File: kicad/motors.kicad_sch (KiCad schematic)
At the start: 71 parts, among them J12 Conn_01x04_Pin, J3 Conn_01x04_Pin, J4 Conn_01x04_Pin, J5 Conn_01x04_Pin, J6 Conn_01x04_Pin, U3 TMC2209-LA, U4 TMC2209-LA, U5 TMC2209-LA, U6 TMC2100-LA

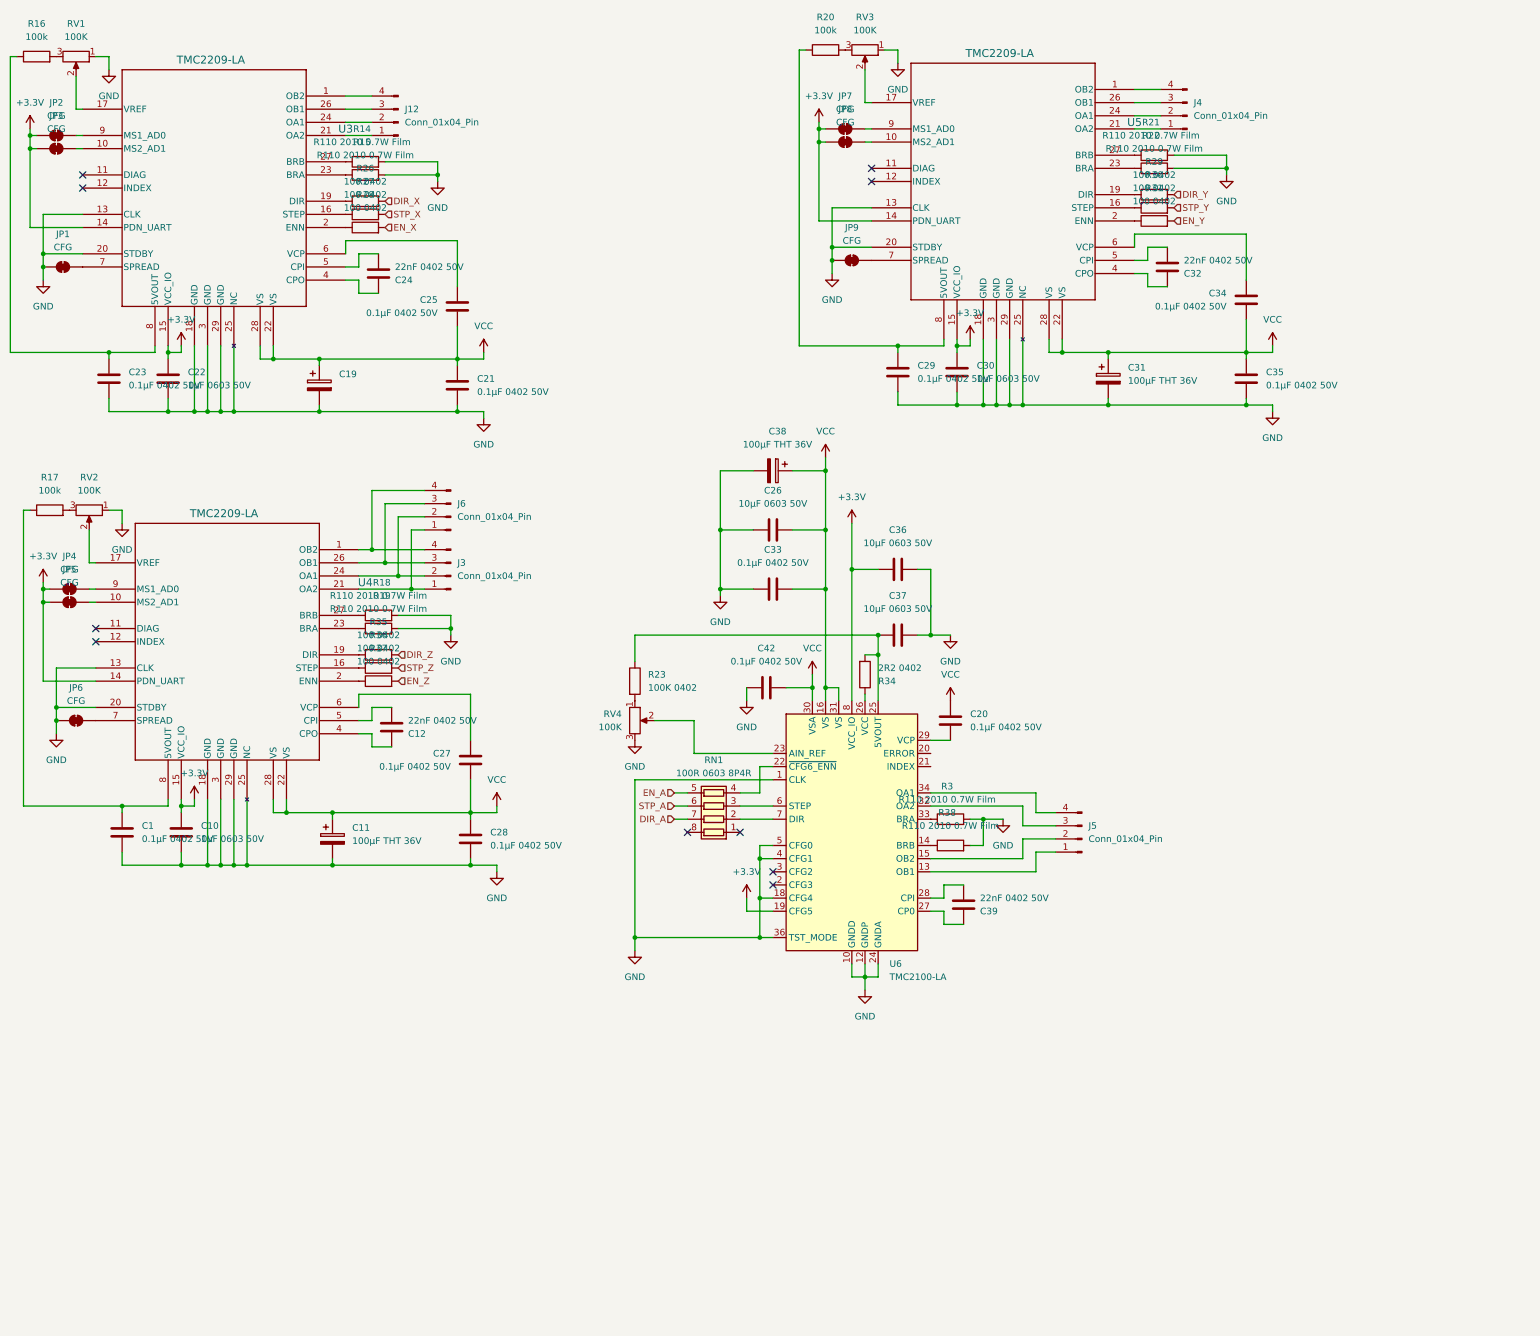
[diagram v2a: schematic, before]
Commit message: DRV8825 schematic
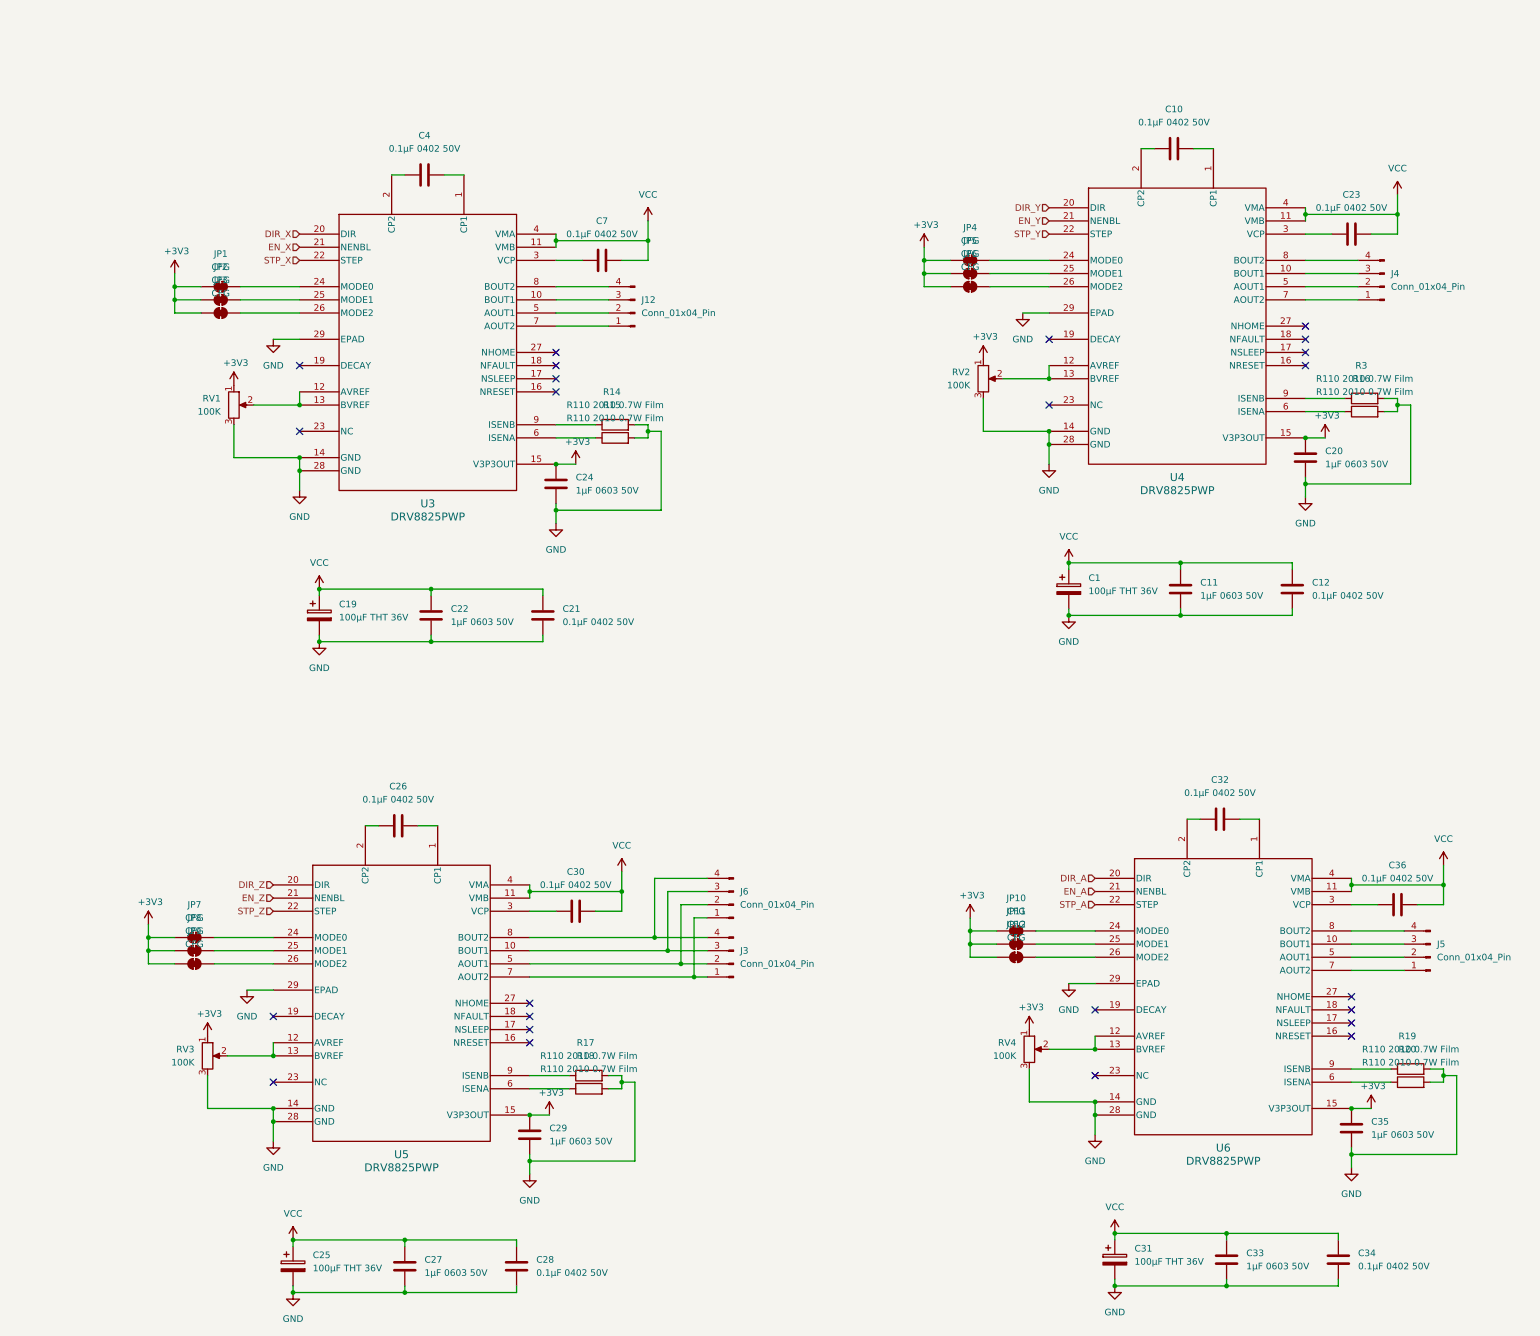
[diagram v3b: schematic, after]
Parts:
- removed C1, C25, C42: 0.1μF 0402 50V, Capacitor_SMD:C_0402_1005Metric, symbol Device:C
- removed C11, C38: 100μF THT 36V, Capacitor_THT:C_Radial_D6.3mm_H11.0mm_P2.50mm, symbol Device:C_Polarized
- removed C37: 10μF 0603 50V, Capacitor_SMD:C_0402_1005Metric, symbol Device:C
- removed C39: 22nF 0402 50V, Capacitor_SMD:C_0402_1005Metric, symbol Device:C
- removed R21, R22, R38: R110 2010 0.7W Film, Resistor_SMD:R_2010_5025Metric, symbol Device:R
- removed R23: 100K 0402, Resistor_SMD:R_0402_1005Metric, symbol Device:R
- removed R26, R27, R28, R29, R30, R31, R35, R36, R37: 100 0402, Resistor_SMD:R_0402_1005Metric, symbol Device:R
- removed R34: 2R2 0402, Resistor_SMD:R_0402_1005Metric, symbol Device:R
- removed RN1: 100R 0603 8P4R, Resistor_SMD:R_Array_Concave_4x0603, symbol Device:R_Pack04
- removed U3, U4, U5: TMC2209-LA, rephat-parts:QFN28_5X5_TRI-M, symbol rephat-symbols:TMC2209-LA
- removed U6: TMC2100-LA, Package_DFN_QFN:QFN-36-1EP_5x6mm_P0.5mm_EP3.6x4.1mm_ThermalVias, symbol Driver_Motor:TMC2100-LA
- added C1, C25: 100μF THT 36V, Capacitor_THT:C_Radial_D6.3mm_H11.0mm_P2.50mm, symbol Device:C_Polarized
- added C11: 1μF 0603 50V, Capacitor_SMD:C_0402_1005Metric, symbol Device:C
- added C4, C7: 0.1μF 0402 50V, Capacitor_SMD:C_0402_1005Metric, symbol Device:C
- added JP10, JP11, JP12: CFG, Jumper:SolderJumper-2_P1.3mm_Bridged_RoundedPad1.0x1.5mm, symbol Jumper:SolderJumper_2_Bridged
- added U3, U4, U5, U6: DRV8825PWP, Package_SO:HTSSOP-28-1EP_4.4x9.7mm_P0.65mm_EP3.4x9.5mm_ThermalVias, symbol rephat-symbols:DRV8825PWP
- C10, C30: value 1μF 0603 50V -> 0.1μF 0402 50V
- C12, C32: value 22nF 0402 50V -> 0.1μF 0402 50V
- C20, C27, C29, C33, C35: value 0.1μF 0402 50V -> 1μF 0603 50V
- C24: value 22nF 0402 50V -> 1μF 0603 50V
- C26, C36: value 10μF 0603 50V -> 0.1μF 0402 50V
- R16, R17, R20: value 100k -> R110 2010 0.7W Film; footprint Resistor_SMD:R_0402_1005Metric -> Resistor_SMD:R_2010_5025Metric
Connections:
- net DIR_A: now also U6.20 (DIR)
- net DIR_X: now also U3.20 (DIR)
- net DIR_Y: now also U4.20 (DIR)
- net DIR_Z: now also U5.20 (DIR)
- net EN_A: now also U6.21 (NENBL)
- net EN_X: now also U3.21 (NENBL)
- net EN_Y: now also U4.21 (NENBL)
- net EN_Z: now also U5.21 (NENBL)
- net GND: now also C12.2, C20.2, C24.2, C27.2, C33.2, C34.2, R16.2, R17.2, R20.2, RV1.3, RV2.3, RV3.3, C1.2, C11.2, C25.2, U3.14 (GND), U3.28 (GND), U3.29 (EPAD), U4.14 (GND), U4.28 (GND), U4.29 (EPAD), U5.14 (GND), U5.28 (GND), U5.29 (EPAD), U6.14 (GND), U6.28 (GND), U6.29 (EPAD); no longer C10.2, C23.2, C26.1, C30.2, C33.1, C36.2, JP1.1 (A), JP6.1 (A), JP9.1 (A), RV1.1, RV2.1, RV3.1
- net STP_A: now also U6.22 (STEP)
- net STP_X: now also U3.22 (STEP)
- net STP_Y: now also U4.22 (STEP)
- net STP_Z: now also U5.22 (STEP)
- net VCC: now also C12.1, C22.1, C23.2, C30.2, C33.1, C36.2, C1.1, C11.1, C25.1, C7.2, U3.11 (VMB), U3.4 (VMA), U4.11 (VMB), U4.4 (VMA), U5.11 (VMB), U5.4 (VMA), U6.11 (VMB), U6.4 (VMA); no longer C20.2, C26.2, C33.2, C35.1
- net at R17.1: now also U5.9 (ISENB)
- net at R3.1: now also U4.9 (ISENB)
- net at J3.1 (Pin_1), J6.1 (Pin_1): now also U5.7 (AOUT2)
- net at J3.2 (Pin_2), J6.2 (Pin_2): now also U5.5 (AOUT1)
- net at J3.3 (Pin_3), J6.3 (Pin_3): now also U5.10 (BOUT1)
- net at J3.4 (Pin_4), J6.4 (Pin_4): now also U5.8 (BOUT2)
- net at JP7.2 (B): now also U5.24 (MODE0)
- net at RV3.2: now also U5.12 (AVREF), U5.13 (BVREF)
- net at RV1.2: now also U3.12 (AVREF), U3.13 (BVREF)
- net at R19.1: now also U6.9 (ISENB)
- net at JP6.2 (B): now also U4.26 (MODE2)
- net at C32.1: now also U6.2 (CP2)
- net at C32.2: now also U6.1 (CP1)
- net at R15.1: now also U3.6 (ISENA)
- net at JP1.2 (B): now also U3.24 (MODE0)
- net at C23.1: now also U4.3 (VCP); no longer R16.1
- net at R20.1: now also U6.6 (ISENA); no longer C29.1
- net +3V3: now reaches C20.1
- net +3V3: now also C24.1, C29.1, C35.1, JP1.1 (A), JP2.1 (A), JP3.1 (A), JP4.1 (A), JP5.1 (A), JP6.1 (A), JP7.1 (A), JP8.1 (A), JP9.1 (A), RV1.1, RV2.1, RV3.1, RV4.1, JP10.1 (A), JP11.1 (A), JP12.1 (A), U3.15 (V3P3OUT), U4.15 (V3P3OUT), U5.15 (V3P3OUT), U6.15 (V3P3OUT)
- net at J12.4 (Pin_4): now also U3.8 (BOUT2)
- net at JP3.2 (B): now also U3.26 (MODE2)
- net at J12.1 (Pin_1): now also U3.7 (AOUT2)
- net at J12.2 (Pin_2): now also U3.5 (AOUT1)
- net at J12.3 (Pin_3): now also U3.10 (BOUT1)
- net at R14.1: now also U3.9 (ISENB)
- net at JP2.2 (B): now also U3.25 (MODE1)
- net at JP5.2 (B): now also U4.25 (MODE1)
- net at RV2.2: now also U4.12 (AVREF), U4.13 (BVREF)
- net at R18.1: now also U5.6 (ISENA)
- net at JP4.2 (B): now also U4.24 (MODE0)
- net at JP8.2 (B): now also U5.25 (MODE1)
- net at J4.1 (Pin_1): now also U4.7 (AOUT2)
- net at J4.2 (Pin_2): now also U4.5 (AOUT1)
- net at J4.3 (Pin_3): now also U4.10 (BOUT1)
- net at J4.4 (Pin_4): now also U4.8 (BOUT2)
- net at RV4.2: now also U6.12 (AVREF), U6.13 (BVREF)
- net at J5.1 (Pin_1): now also U6.7 (AOUT2)
- net at J5.2 (Pin_2): now also U6.5 (AOUT1)
- net at J5.3 (Pin_3): now also U6.10 (BOUT1)
- net at J5.4 (Pin_4): now also U6.8 (BOUT2)
- net at JP9.2 (B): now also U5.26 (MODE2)
- removed net +3.3V: C10.1, C22.1, C30.1, C36.1, JP2.1 (A), JP3.1 (A), JP4.1 (A), JP5.1 (A), JP7.1 (A), JP8.1 (A)
- new net: C36.1, U6.3 (VCP)
- new net: C10.1, U4.2 (CP2)
- new net: C10.2, U4.1 (CP1)
- new net: C30.1, U5.3 (VCP)
- new net: C26.1, U5.2 (CP2)
- new net: C26.2, U5.1 (CP1)
- new net: JP10.2 (B), U6.24 (MODE0)
- new net: R16.1, U4.6 (ISENA)
- new net: JP11.2 (B), U6.25 (MODE1)
- new net: C4.1, U3.2 (CP2)
- new net: C4.2, U3.1 (CP1)
- new net: JP12.2 (B), U6.26 (MODE2)
- new net: C7.1, U3.3 (VCP)
- no-connect marks 10 -> 24
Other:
- moved on the sheet: C19, C21, C22, J12, J3, J4, J5, J6, RV1

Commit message: PCB redo
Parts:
- R14, R15, R16, R17, R18, R19, R20, R3: value R110 2010 0.7W Film -> R100 0603; footprint Resistor_SMD:R_2010_5025Metric -> Resistor_SMD:R_0603_1608Metric
- RV1, RV2, RV3, RV4: value 100K -> 10K
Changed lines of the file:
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@@
 			)
 		)
-		(property "Value" "100K"
+		(property "Value" "10K"
 			(at 62.23 93.9799 0)
 			(effects
@@
 			)
 		)
-		(property "Value" "R110 2010 0.7W Film"
+		(property "Value" "R100 0603"
 			(at 138.43 92.71 90)
 			(effects
@@
 			)
 		)
-		(property "Footprint" "Resistor_SMD:R_2010_5025Metric"
+		(property "Footprint" "Resistor_SMD:R_0603_1608Metric"
 			(at 138.43 98.298 90)
 			(effects
@@
 			)
 		)
-		(property "Value" "100K"
+		(property "Value" "10K"
 			(at 57.15 219.7099 0)
 			(effects
@@
 			)
 		)
-		(property "Value" "R110 2010 0.7W Film"
+		(property "Value" "R100 0603"
 			(at 133.35 218.44 90)
 			(effects
@@
 			)
 		)
-		(property "Footprint" "Resistor_SMD:R_2010_5025Metric"
+		(property "Footprint" "Resistor_SMD:R_0603_1608Metric"
 			(at 133.35 224.028 90)
 			(effects
@@
 			)
 		)
-		(property "Value" "100K"
+		(property "Value" "10K"
 			(at 215.9 218.4399 0)
 			(effects
@@
 			)
 		)
-		(property "Value" "R110 2010 0.7W Film"
+		(property "Value" "R100 0603"
 			(at 133.35 220.98 90)
 			(effects
@@
 			)
 		)
-		(property "Footprint" "Resistor_SMD:R_2010_5025Metric"
+		(property "Footprint" "Resistor_SMD:R_0603_1608Metric"
 			(at 133.35 226.568 90)
 			(effects
@@
 			)
 		)
-		(property "Value" "R110 2010 0.7W Film"
+		(property "Value" "R100 0603"
 			(at 138.43 95.25 90)
 			(effects
@@
 			)
 		)
-		(property "Footprint" "Resistor_SMD:R_2010_5025Metric"
+		(property "Footprint" "Resistor_SMD:R_0603_1608Metric"
 			(at 138.43 100.838 90)
 			(effects
@@
 			)
 		)
-		(property "Value" "R110 2010 0.7W Film"
+		(property "Value" "R100 0603"
 			(at 292.1 219.71 90)
 			(effects
@@
 			)
 		)
-		(property "Footprint" "Resistor_SMD:R_2010_5025Metric"
+		(property "Footprint" "Resistor_SMD:R_0603_1608Metric"
 			(at 292.1 225.298 90)
 			(effects
@@
 			)
 		)
-		(property "Value" "R110 2010 0.7W Film"
+		(property "Value" "R100 0603"
 			(at 283.21 90.17 90)
 			(effects
@@
 			)
 		)
-		(property "Footprint" "Resistor_SMD:R_2010_5025Metric"
+		(property "Footprint" "Resistor_SMD:R_0603_1608Metric"
 			(at 283.21 95.758 90)
 			(effects
@@
 			)
 		)
-		(property "Value" "R110 2010 0.7W Film"
+		(property "Value" "R100 0603"
 			(at 292.1 217.17 90)
 			(effects
@@
 			)
 		)
-		(property "Footprint" "Resistor_SMD:R_2010_5025Metric"
+		(property "Footprint" "Resistor_SMD:R_0603_1608Metric"
 			(at 292.1 222.758 90)
 			(effects
@@
 			)
 		)
-		(property "Value" "R110 2010 0.7W Film"
+		(property "Value" "R100 0603"
 			(at 283.21 87.63 90)
 			(effects
@@
 			)
 		)
-		(property "Footprint" "Resistor_SMD:R_2010_5025Metric"
+		(property "Footprint" "Resistor_SMD:R_0603_1608Metric"
 			(at 283.21 93.218 90)
 			(effects
@@
 			)
 		)
-		(property "Value" "100K"
+		(property "Value" "10K"
 			(at 207.01 88.8999 0)
 			(effects

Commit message: schematic candidate 0
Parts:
- added RN1, RN2, RN3, RN4: 100R 4x0603, Resistor_SMD:R_Array_Concave_4x0603, symbol Device:R_Pack04
- J12, J3, J4, J5, J6: footprint Connector_JST:JST_XH_B4B-XH-A_1x04_P2.50mm_Vertical -> rephat-parts:S4B-XH-SM4-TB
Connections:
- net DIR_A: now also RN4.6 (R3.2); no longer U6.20 (DIR)
- net DIR_X: now also RN2.6 (R3.2); no longer U3.20 (DIR)
- net DIR_Y: now also RN1.6 (R3.2); no longer U4.20 (DIR)
- net DIR_Z: now also RN3.6 (R3.2); no longer U5.20 (DIR)
- net EN_A: now also RN4.7 (R2.2); no longer U6.21 (NENBL)
- net EN_X: now also RN2.7 (R2.2); no longer U3.21 (NENBL)
- net EN_Y: now also RN1.7 (R2.2); no longer U4.21 (NENBL)
- net EN_Z: now also RN3.7 (R2.2); no longer U5.21 (NENBL)
- net STP_A: now also RN4.8 (R1.2); no longer U6.22 (STEP)
- net STP_X: now also RN2.8 (R1.2); no longer U3.22 (STEP)
- net STP_Y: now also RN1.8 (R1.2); no longer U4.22 (STEP)
- net STP_Z: now also RN3.8 (R1.2); no longer U5.22 (STEP)
- new net: RN4.1 (R1.1), U6.22 (STEP)
- new net: RN4.2 (R2.1), U6.21 (NENBL)
- new net: RN4.3 (R3.1), U6.20 (DIR)
- new net: RN3.1 (R1.1), U5.22 (STEP)
- new net: RN3.2 (R2.1), U5.21 (NENBL)
- new net: RN3.3 (R3.1), U5.20 (DIR)
- new net: RN1.1 (R1.1), U4.22 (STEP)
- new net: RN1.2 (R2.1), U4.21 (NENBL)
- new net: RN1.3 (R3.1), U4.20 (DIR)
- new net: RN2.1 (R1.1), U3.22 (STEP)
- new net: RN2.2 (R2.1), U3.21 (NENBL)
- new net: RN2.3 (R3.1), U3.20 (DIR)
- no-connect marks 24 -> 32
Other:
- moved on the sheet: C1, C10, C11, C12, C19, C20, C21, C22, C23, C24, C25, C26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

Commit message: Toshiba TB67S109A stepper driver
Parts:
- removed C35: 1μF 0603 50V, Capacitor_SMD:C_0402_1005Metric, symbol Device:C
- removed C36: 0.1μF 0402 50V, Capacitor_SMD:C_0402_1005Metric, symbol Device:C
- removed R20: R100 0603, Resistor_SMD:R_0603_1608Metric, symbol Device:R
- removed RV4: 10K, Potentiometer_SMD:Potentiometer_Bourns_TC33X_Vertical, symbol Device:R_Potentiometer
- removed U6: DRV8825PWP, Package_SO:HTSSOP-28-1EP_4.4x9.7mm_P0.65mm_EP3.4x9.5mm_ThermalVias, symbol rephat-symbols:DRV8825PWP
- added D6: LED, LED_SMD:LED_0603_1608Metric, symbol Device:LED
- added R11: 20K 0402, Resistor_SMD:R_0402_1005Metric, symbol Device:R
- added R13: 200Ω 0402, Resistor_SMD:R_0402_1005Metric, symbol Device:R
- added RV5: 10K, Potentiometer_SMD:Potentiometer_Bourns_TC33X_Vertical, symbol Device:R_Potentiometer
- added U6: TB67S109AFTG, Package_DFN_QFN:QFN-48-1EP_7x7mm_P0.5mm_EP5.45x5.45mm_ThermalVias, symbol rephat-symbols:TB67S109AFTG
- C32: value 0.1μF 0402 50V -> 100 pF 0402 50V
- R19: value R100 0603 -> 100K 0402; footprint Resistor_SMD:R_0603_1608Metric -> Resistor_SMD:R_0402_1005Metric
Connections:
- net DIR_A: now also RN4.7 (R2.2); no longer RN4.6 (R3.2)
- net EN_A: now also RN4.8 (R1.2); no longer RN4.7 (R2.2)
- net GND: now also C32.2, U6.15 (GND), U6.18 (GND), U6.19 (GND), U6.22 (GND), U6.4 (RESET), U6.40 (GND), U6.5 (GND); no longer R19.2
- net STP_A: now also RN4.6 (R3.2); no longer RN4.8 (R1.2)
- net VCC: now also U6.32 (VM)
- net at RN4.1 (R1.1): now also U6.3 (ENABLE)
- net at RN4.2 (R2.1): now also U6.44 (CW/CCW)
- net at RN4.3 (R3.1): now also U6.2 (CLK)
- net at JP10.2 (B): now also U6.39 (DMODE0)
- net +5V: now reaches R19.1
- net +5V: now also D6.2 (A), R11.1, U6.34 (VCC)
- net at J5.1 (Pin_1): now also U6.16 (OUTA-), U6.17 (OUTA-)
- net at J5.2 (Pin_2): now also U6.10 (OUTA+), U6.11 (OUTA+)
- net at J5.3 (Pin_3): now also U6.26 (OUTB+), U6.27 (OUTB+)
- net at J5.4 (Pin_4): now also U6.20 (OUTB-), U6.21 (OUTB-)
- net at JP11.2 (B): now also U6.46 (DMODE1)
- net at JP12.2 (B): now also U6.47 (DMODE2)
- net at C32.1: now also R11.2, U6.43 (OSCM)
- new net: R13.1, R19.2, U6.38 (LO)
- new net: D6.1 (K), R13.2
- no-connect marks 32 -> 27
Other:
- moved on the sheet: C31, C33, C34, J5, JP10, JP11, JP12, RN4
